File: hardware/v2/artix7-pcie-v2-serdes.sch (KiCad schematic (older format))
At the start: 22 parts, among them J4 USB3_A, J5 USB3_A, U1 XC7A75T-FGG484

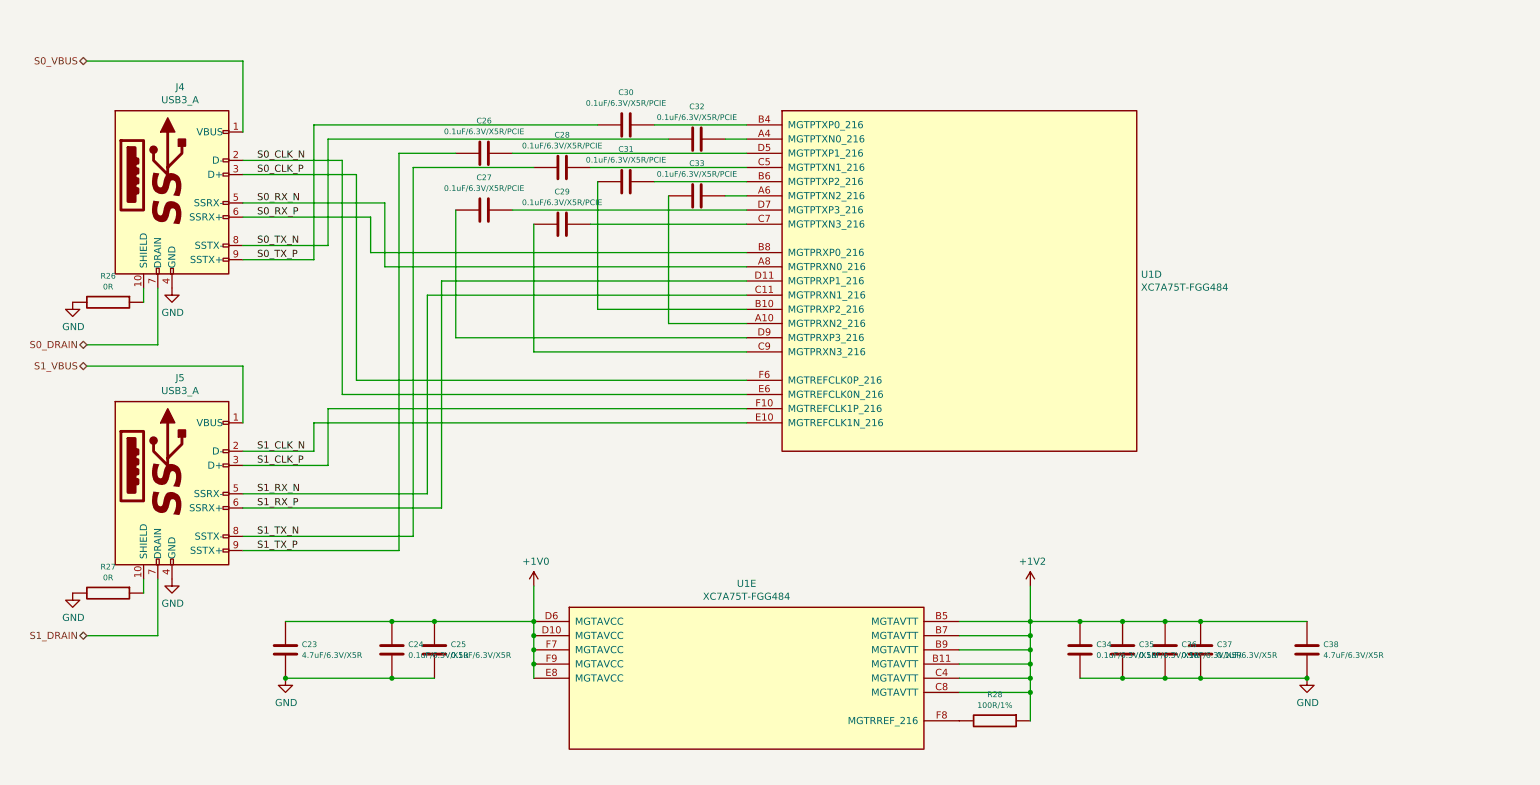
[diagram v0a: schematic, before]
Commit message: v2 hardware - all io connectors in schematic
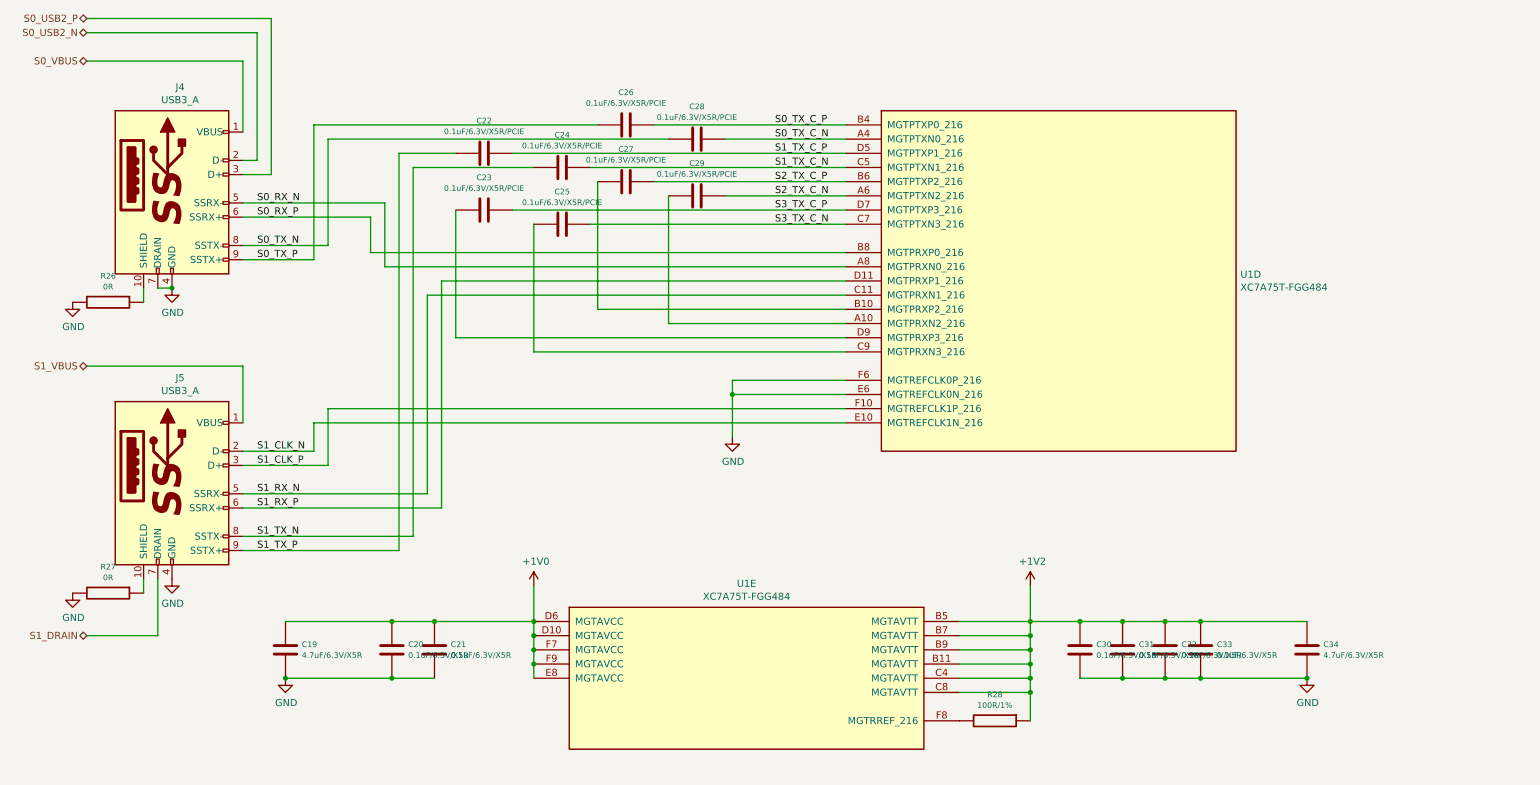
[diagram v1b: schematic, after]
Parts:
- J4, J5: footprint (none) -> tom-connectors:USB3_A_Aliexpress
- U1: footprint (none) -> artix7-pcie-v2:Xilinx_FGG484
- renumbered C23 to C19, C24 to C20, C25 to C21, C26 to C22, C27 to C23, C28 to C24, C29 to C25, C30 to C26, C31 to C27, C32 to C28, C33 to C29, C34 to C30, C35 to C31, C36 to C32, C37 to C33, C38 to C34
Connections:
- net S0_DRAIN is gone; now on net GND: J4.7 (DRAIN)
- net GND: now also U1.E6 (MGTREFCLK0N_216), U1.F6 (MGTREFCLK0P_216)
- net S1_TX_C_P: now reaches C22.1, U1.D5 (MGTPTXP1_216)
- net S1_TX_C_N: now reaches C24.1, U1.C5 (MGTPTXN1_216)
- net S2_TX_C_N: now reaches C29.1, U1.A6 (MGTPTXN2_216)
- net S2_TX_C_P: now reaches C27.1, U1.B6 (MGTPTXP2_216)
- net S3_TX_C_N: now reaches C25.1, U1.C7 (MGTPTXN3_216)
- net S3_TX_C_P: now reaches C23.1, U1.D7 (MGTPTXP3_216)
- net S0_TX_C_N: now reaches C28.1, U1.A4 (MGTPTXN0_216)
- net S0_TX_C_P: now reaches C26.1, U1.B4 (MGTPTXP0_216)
- net S0_CLK_N renamed S0_USB2_N
- net S0_USB2_N: no longer U1.E6 (MGTREFCLK0N_216)
- net S0_CLK_P renamed S0_USB2_P
- net S0_USB2_P: no longer U1.F6 (MGTREFCLK0P_216)
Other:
- moved on the sheet: U1D

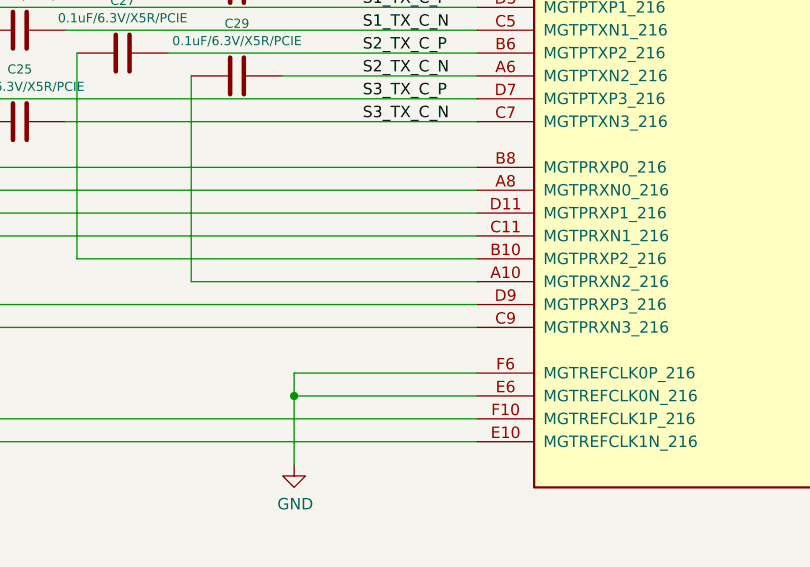
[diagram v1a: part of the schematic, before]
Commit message: v2 schematic/pcb: band 13 to NC for smaller device compatibility
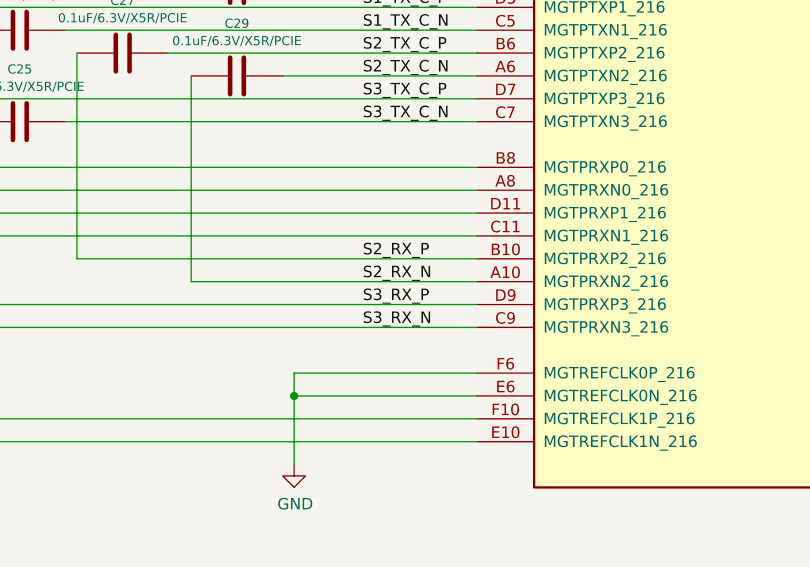
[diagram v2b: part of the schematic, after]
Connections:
- net S2_RX_N: now reaches C29.2, U1.A10 (MGTPRXN2_216)
- net S2_RX_P: now reaches C27.2, U1.B10 (MGTPRXP2_216)
- net S3_RX_N: now reaches C25.2, U1.C9 (MGTPRXN3_216)
- net S3_RX_P: now reaches C23.2, U1.D9 (MGTPRXP3_216)
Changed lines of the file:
@@
 $Descr A4 11693 8268
 encoding utf-8
-Sheet 4 6
+Sheet 4 7
 Title ""
 Date ""
@@
 Text Label 5950 2500 0    50   ~ 0
 S3_TX_C_N
+Text Label 5950 3200 0    50   ~ 0
+S2_RX_N
+Text Label 5950 3100 0    50   ~ 0
+S2_RX_P
+Text Label 5950 3300 0    50   ~ 0
+S3_RX_P
+Text Label 5950 3400 0    50   ~ 0
+S3_RX_N
 $EndSCHEMATC

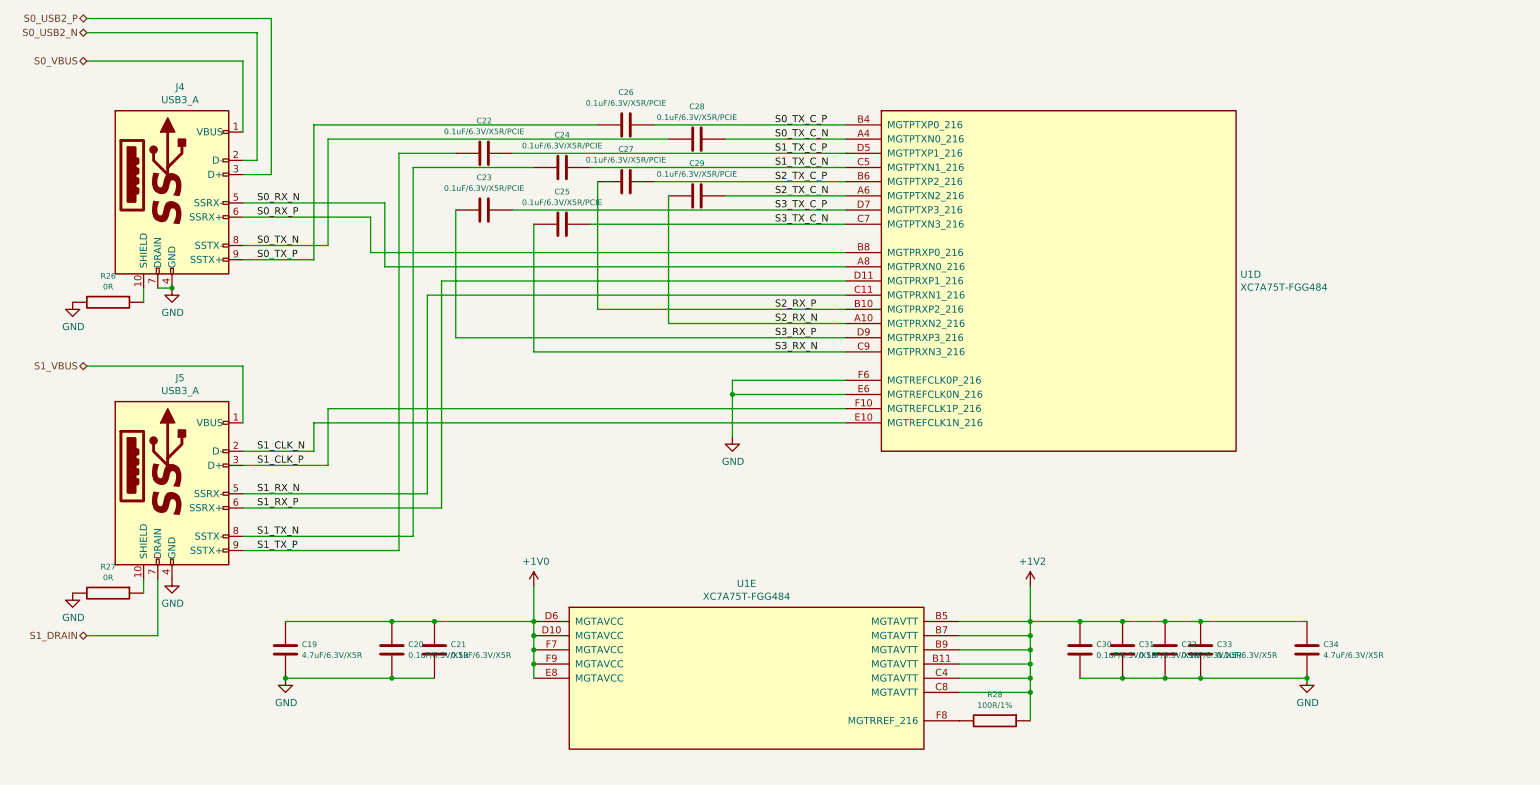
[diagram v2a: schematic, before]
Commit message: v2 hardware progress checkin, just prior to replacing p/s with TI parts
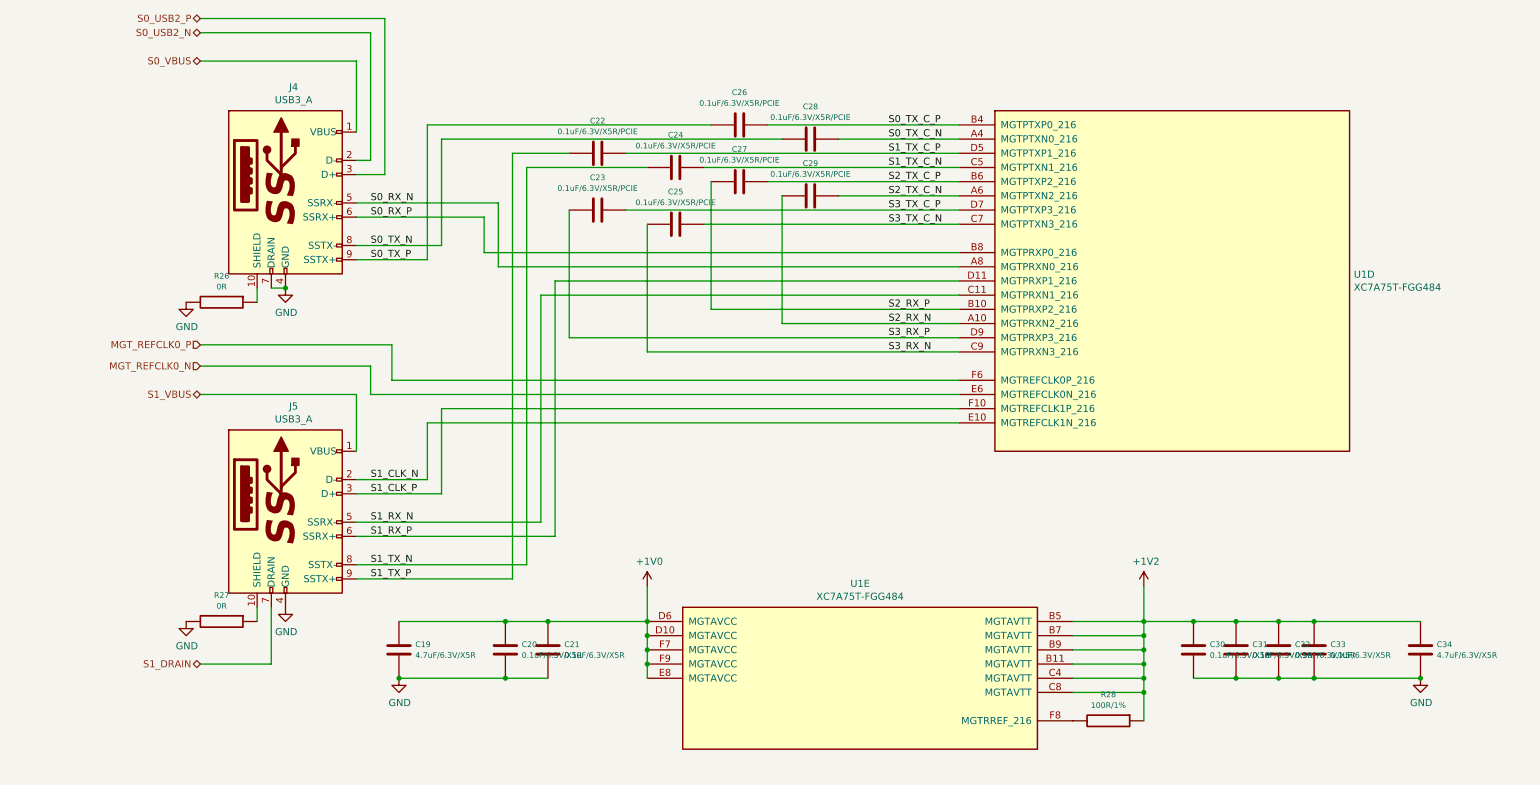
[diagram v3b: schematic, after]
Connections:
- net GND: no longer U1.E6 (MGTREFCLK0N_216), U1.F6 (MGTREFCLK0P_216)
- new net MGT_REFCLK0_N: U1.E6 (MGTREFCLK0N_216)
- new net MGT_REFCLK0_P: U1.F6 (MGTREFCLK0P_216)
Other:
- moved on the sheet: C19, C20, C21, C22, C23, C24, C25, C26, C27, C28, C29, C30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
